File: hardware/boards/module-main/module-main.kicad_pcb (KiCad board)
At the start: 4 copper layers, 48.5 x 108.5 mm, 177 parts, among them J1 2x8 2.54mm shrouded box heade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, J2 2x10 2.54mm pin header, J3 Neutrik NE8FAV, J4 JST B2B-XH-A, Q1 PSMN2R0-30YLE, SW1 NKK M2011SD4G01, U1 LT3042EMSE, U10 OPA2197, U11 OPA2197, U12 OPA2197, U13 ADP7118AUJZ-5.0, U14 RPA20-2412SAW, U15 74AHCT14, U2 LT1641-1IS8, U3 DAC8568ICPW, U4 74AHCT125, U5 OPA2197, U6 INA828IDR, U7 OPA2197, U8 OPA2197IDR, U9 OPA2197

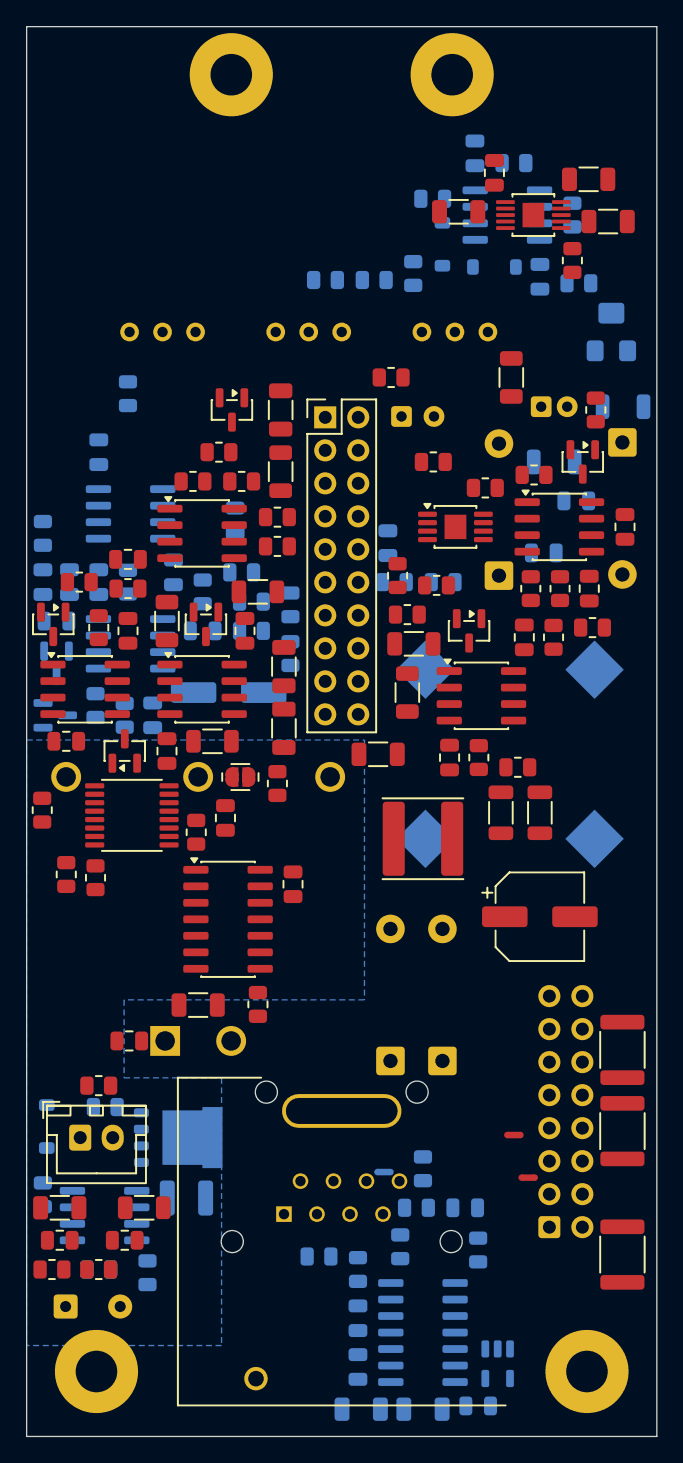
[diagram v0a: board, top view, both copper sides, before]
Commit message: module-main: re-placed - breath receive at the top beside its trimmer, the DAC's LDO beside the DAC, parts spread for routing; placement DRC-clean
Co-Authored-By: Claude Opus 5.5 <noreply@anthropic.com>
Claude-Session: https://claude.ai/code/session_01LmB4muFXnoLprWX4JzuJ5A
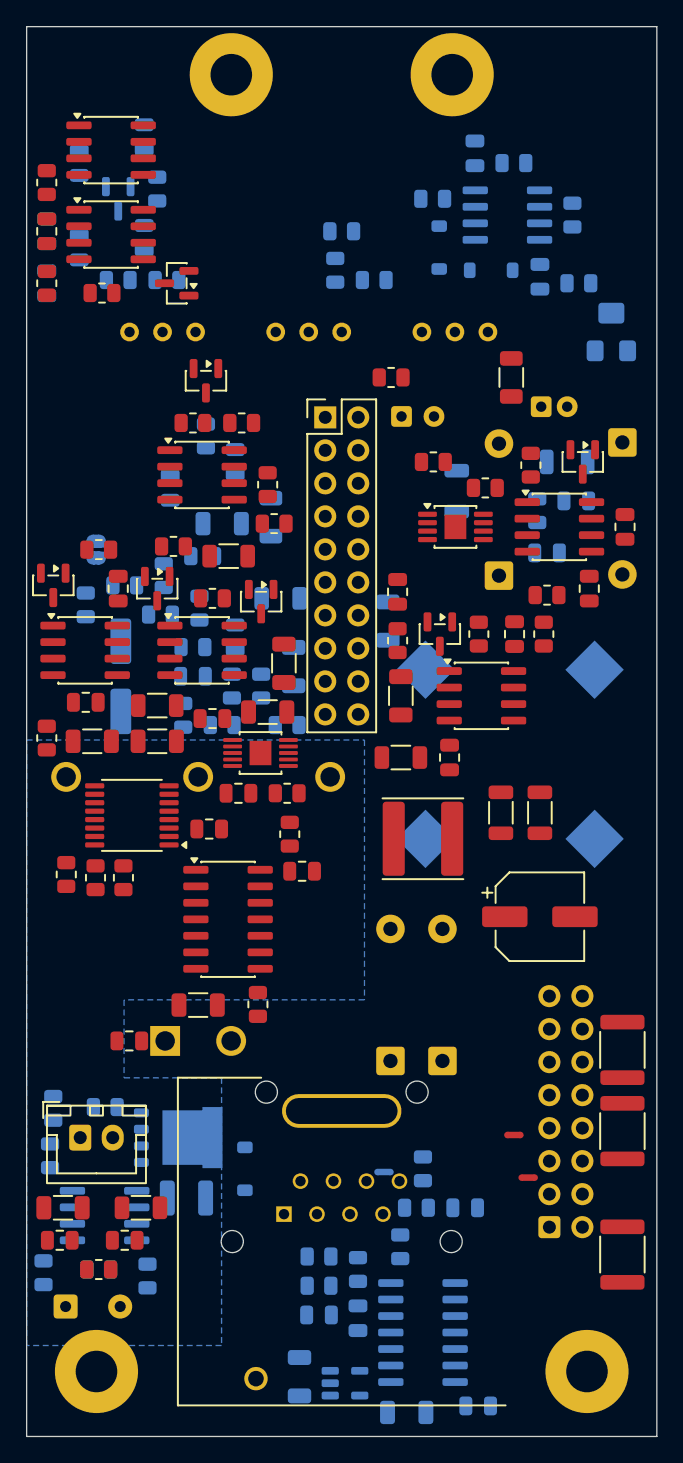
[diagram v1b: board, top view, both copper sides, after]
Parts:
- C13, C29, C43, D4, R16, R17, R19, R40, U5, U6: moved to F.Cu
- C21, C22, C30, C31, C36, C38, JP1, R25, R26, R35, R36, R37, R38, R41, R47, R53, R58, R64, R71: moved to B.Cu
- moved C5 56.4 mm to (66.0, 86.5), turned to 180 degrees
- moved R1 54.7 mm to (62.5, 86.2), turned to 90 degrees
- moved C6 54.5 mm to (71.0, 86.5), turned to 180 degrees
- moved C7 47.3 mm to (75.3, 84.8), turned to 180 degrees
- moved U1 46.4 mm to (79.0, 87.4)
- moved C51 41.2 mm to (79.5, 84.2), turned to 0 degrees
- moved D5 36.1 mm to (68.0, 44.8)
- moved D4 34.5 mm to (72.5, 51.2), turned to 180 degrees
- moved C18 33.6 mm to (70.0, 40.0)
- moved R17 32.7 mm to (62.5, 51.2)
- moved R16 32.5 mm to (66.8, 52.0), turned to 180 degrees
- moved U6 31.5 mm to (67.5, 47.5)
- moved R19 31.4 mm to (62.5, 43.5)
- moved R20 31.2 mm to (71.0, 44.0)
- moved C16 30.6 mm to (70.0, 47.8), turned to -90 degrees
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
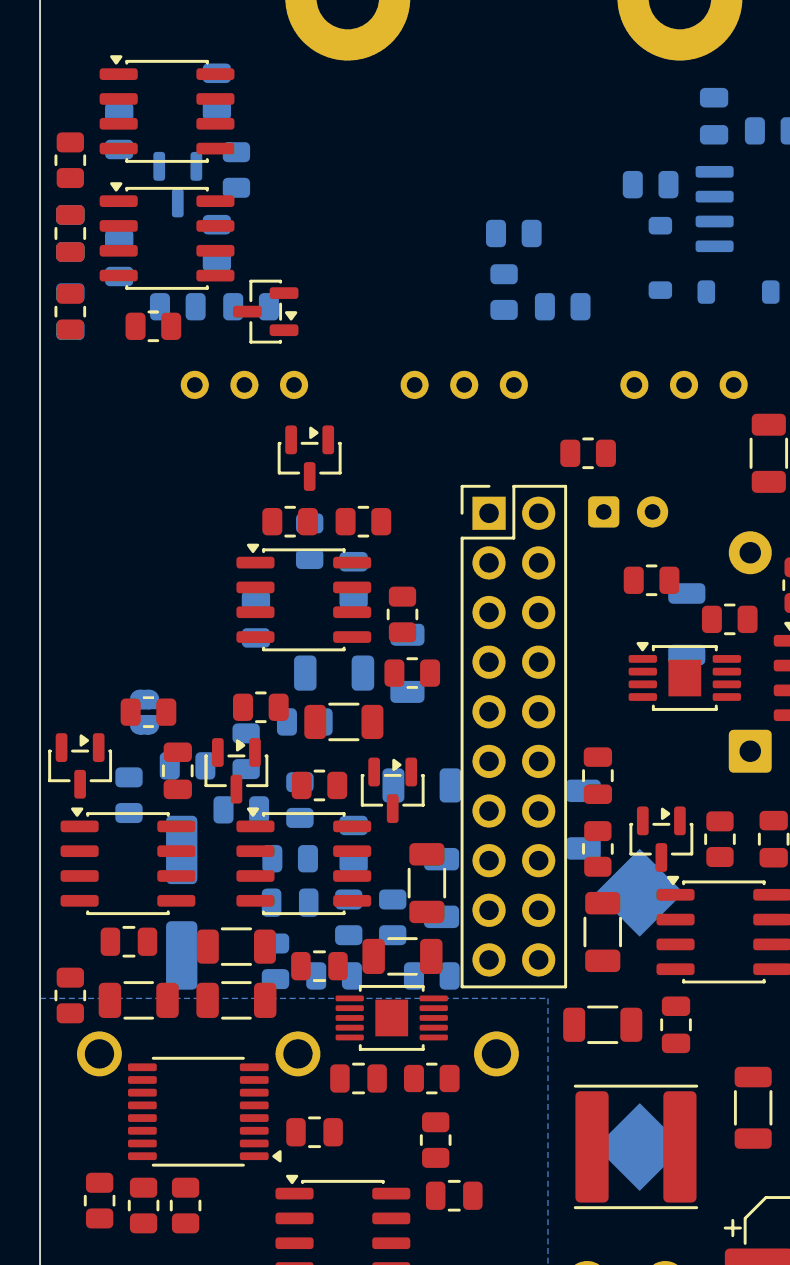
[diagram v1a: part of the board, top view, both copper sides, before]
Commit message: module-main: LDO block to the top middle (R-SET-DAC away from edges, standoffs, connectors; along the long edge), SET guard on both faces, DAC decouplers at their pins
Co-Authored-By: Claude Opus 5.5 <noreply@anthropic.com>
Claude-Session: https://claude.ai/code/session_01LmB4muFXnoLprWX4JzuJ5A
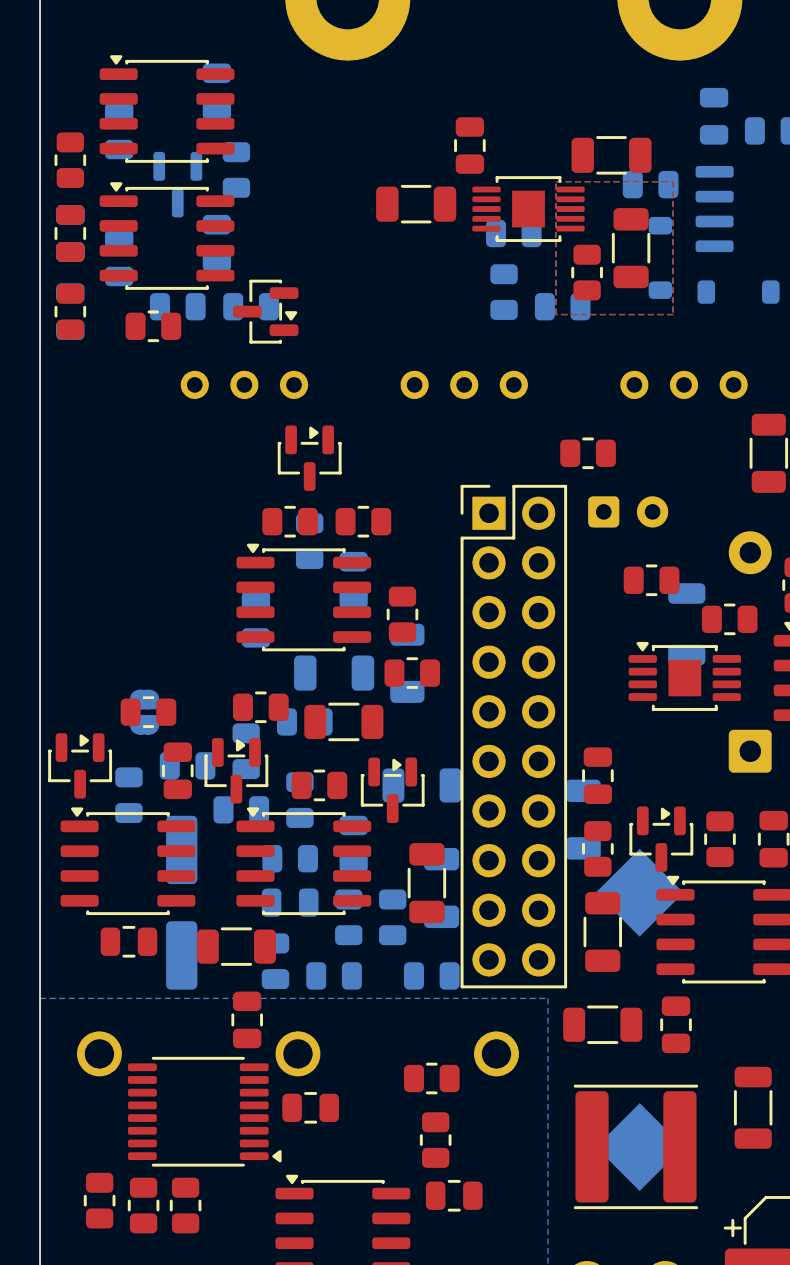
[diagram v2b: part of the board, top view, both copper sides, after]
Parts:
- moved C6 47.3 mm to (90.2, 43.2), turned to 0 degrees
- moved C5 46.0 mm to (91.2, 48.0), turned to -90 degrees
- moved R1 45.5 mm to (89.0, 49.2), turned to -90 degrees
- moved C7 42.7 mm to (83.0, 42.8), turned to 90 degrees
- moved U1 42.0 mm to (86.0, 46.0)
- moved C51 38.5 mm to (80.2, 45.8), turned to 180 degrees
- moved C43 6.44 mm to (71.6, 87.5), turned to 90 degrees
- moved C11 1.27 mm to (74.8, 92.0)
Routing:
- added copper zone on B.Cu, net /DAC_AVDD
- added copper zone on F.Cu, net /DAC_AVDD

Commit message: module-main: routing in progress (resumable run's saved state)
Co-Authored-By: Claude Opus 5.5 <noreply@anthropic.com>
Claude-Session: https://claude.ai/code/session_01LmB4muFXnoLprWX4JzuJ5A
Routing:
- net /AGND_SENSE: track 0.00 -> 89.5 mm
- net AGND_MOD: track 0.00 -> 86.1 mm, vias 0 -> 59
- net /BREATH_SENSE: track 0.00 -> 85.8 mm
- net /DAC_AVDD: track 0.00 -> 80.7 mm, vias 0 -> 8
- net MODULE_ANALOG_POS12: track 0.00 -> 38.7 mm, vias 0 -> 32
- net DIG_GND: track 0.00 -> 21.8 mm, vias 0 -> 21
- net /mod-channels/OUT_1: track 0.00 -> 18.8 mm, vias 0 -> 4
- net PWR_GND: track 0.00 -> 13.4 mm, vias 0 -> 3
- net /mod-channels/VREF_MOD: track 0.00 -> 8.21 mm, vias 0 -> 2
- net /breath-receive-stage/IN_NEG: track 0.00 -> 7.55 mm, vias 0 -> 2
- net MODULE_ANALOG_NEG12: track 0.00 -> 6.26 mm
- net /power-entry/BUS_GND: track 0.00 -> 5.73 mm
- net LOGIC_5V: track 0.00 -> 5.08 mm
- net /PITCH_JACK: track 0.00 -> 4.11 mm
- net /GAIN_FLOOR: track 0.00 -> 3.98 mm, vias 0 -> 1
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
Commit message: module-main: routing in progress (94 connections left); pcb_route.escape for fine-pitch pads
Co-Authored-By: Claude Opus 5.5 <noreply@anthropic.com>
Claude-Session: https://claude.ai/code/session_01LmB4muFXnoLprWX4JzuJ5A
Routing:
- net MODULE_ANALOG_NEG12: track 6.26 -> 181.0 mm, vias 0 -> 21
- net /DAC_AVDD: track 80.7 -> 205.3 mm, vias 8 -> 18
- net LOGIC_5V: track 5.08 -> 49.5 mm, vias 0 -> 6
- net /dac8568/CLR: track 0.00 -> 38.0 mm, vias 0 -> 4
- net /mod-channels/OUT_4: track 1.00 -> 23.5 mm, vias 0 -> 6
- net /mod-channels/MINUS_3: track 1.00 -> 22.6 mm, vias 0 -> 3
- net /UMBILICAL_POS12: track 2.38 -> 23.7 mm, vias 0 -> 7
- net MODULE_ANALOG_POS12: track 38.7 -> 59.3 mm, vias 32 -> 34
- net /digital-and-supervision/SCLK_RC: track 1.33 -> 21.9 mm, vias 0 -> 4
- net /mod-channels/OUT_3: track 0.00 -> 19.7 mm, vias 0 -> 2
- net /pitch-stage/AMP_OUT: track 1.33 -> 18.7 mm, vias 0 -> 2
- net /digital-and-supervision/MOSI_RC: track 0.00 -> 15.6 mm, vias 0 -> 6
- net /umbilical-load-switch/SENSE_NODE: track 1.97 -> 16.5 mm, vias 1 -> 3
- net /breath-output-stage/BREATH_OUT: track 1.45 -> 15.8 mm, vias 1 -> 5
- net /pitch-stage/VREF_SUM: track 0.00 -> 12.3 mm, vias 0 -> 2
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
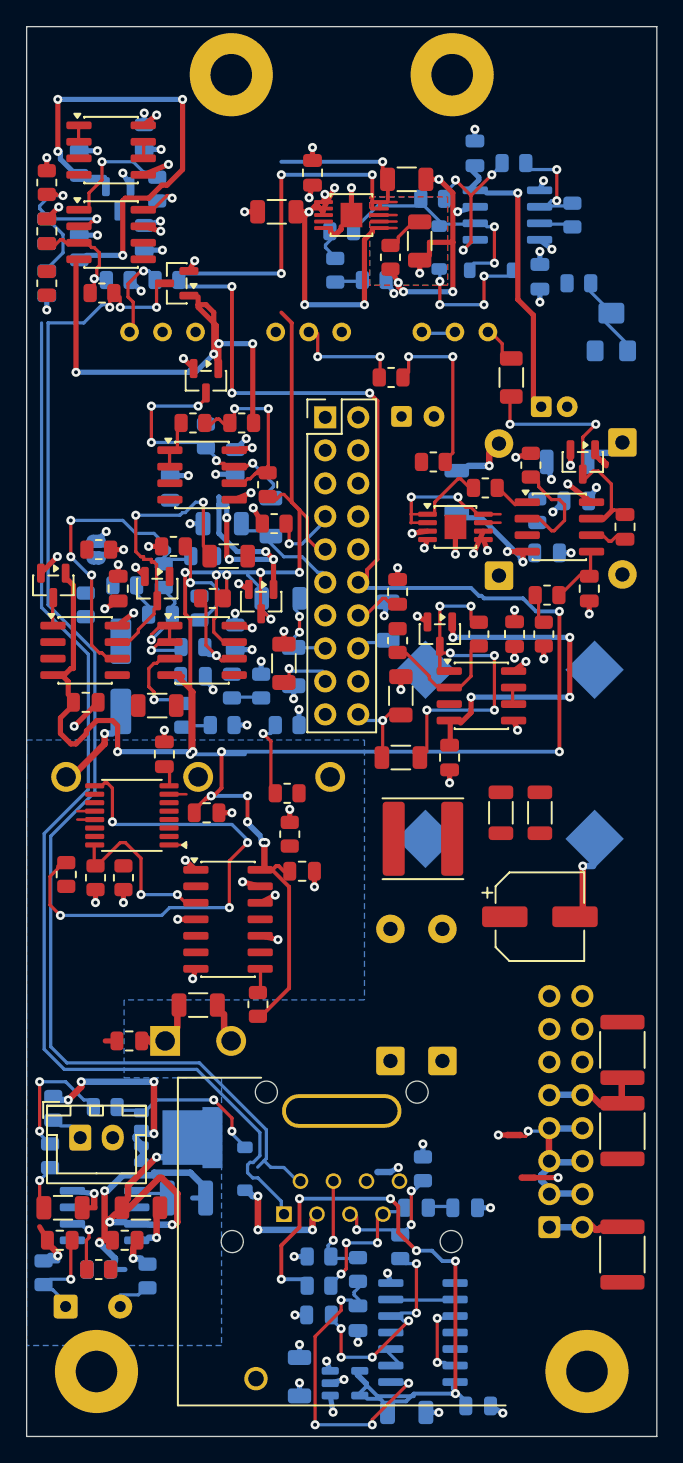
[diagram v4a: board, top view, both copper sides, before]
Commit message: pcb_route: complete routes layer 3 too when layout.yaml directions: names it; module-main routed by it on three directional layers
Co-Authored-By: Claude Opus 5.5 <noreply@anthropic.com>
Claude-Session: https://claude.ai/code/session_01LmB4muFXnoLprWX4JzuJ5A
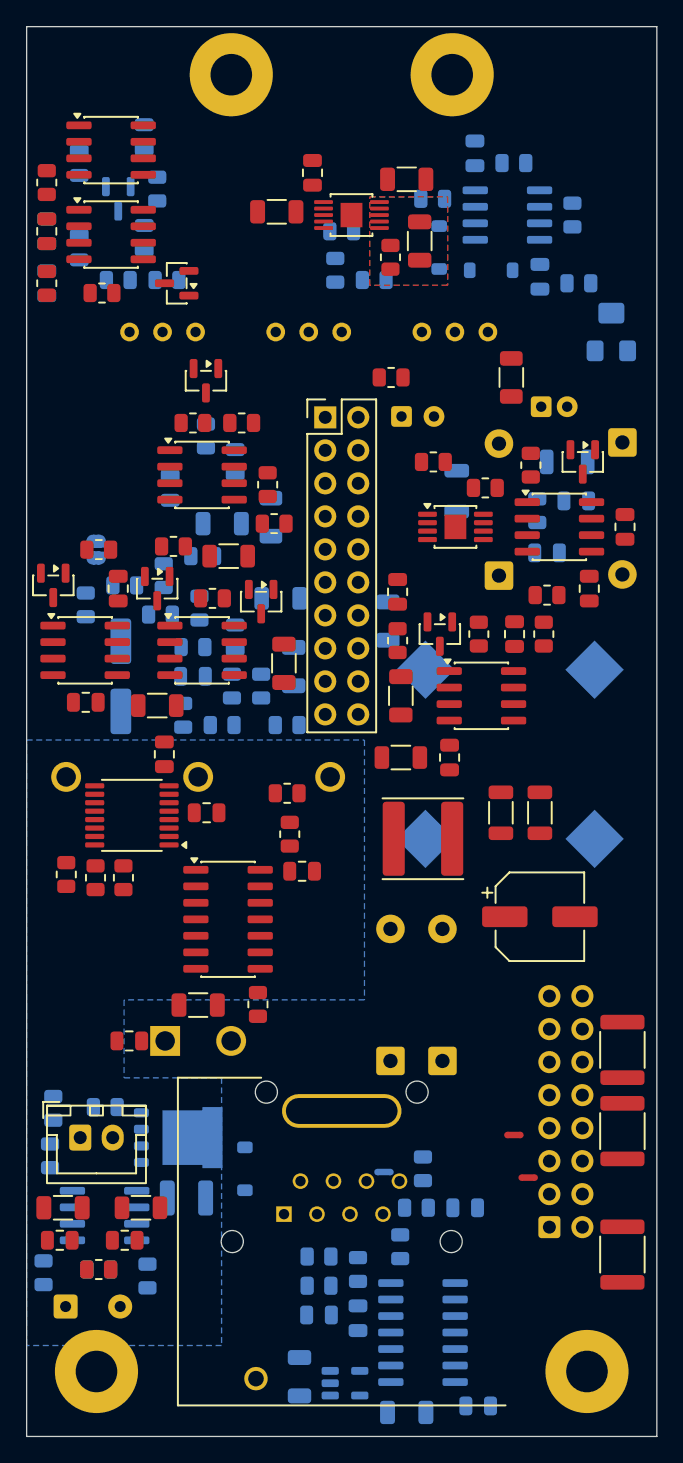
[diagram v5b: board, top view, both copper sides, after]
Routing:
- net /DAC_AVDD: track 205.3 -> 0.00 mm, vias 18 -> 0
- net MODULE_ANALOG_NEG12: track 181.0 -> 0.00 mm, vias 21 -> 0
- net /AGND_SENSE: track 95.1 -> 0.00 mm, vias 3 -> 0
- net AGND_MOD: track 87.5 -> 0.00 mm, vias 59 -> 0
- net /BREATH_SENSE: track 85.8 -> 0.00 mm
- net MODULE_ANALOG_POS12: track 59.3 -> 0.00 mm, vias 34 -> 0
- net LOGIC_5V: track 49.5 -> 0.00 mm, vias 6 -> 0
- net /dac8568/CLR: track 38.0 -> 0.00 mm, vias 4 -> 0
- net PWR_GND: track 25.6 -> 0.00 mm, vias 4 -> 0
- net /UMBILICAL_POS12: track 23.7 -> 0.00 mm, vias 7 -> 0
- net /mod-channels/OUT_4: track 23.5 -> 0.00 mm, vias 6 -> 0
- net /mod-channels/MINUS_3: track 22.6 -> 0.00 mm, vias 3 -> 0
- net /digital-and-supervision/SCLK_RC: track 21.9 -> 0.00 mm, vias 4 -> 0
- net DIG_GND: track 21.8 -> 0.00 mm, vias 21 -> 0
- net /mod-channels/OUT_3: track 19.7 -> 0.00 mm, vias 2 -> 0
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- removed copper zone on In2.Cu, net MODULE_ANALOG_POS12

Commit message: module-main: routing state (three directional layers, in progress); pcb_route: a front and a rear pad at one place get a via, tidy squares outer joins only
Co-Authored-By: Claude Opus 5.5 <noreply@anthropic.com>
Claude-Session: https://claude.ai/code/session_01LmB4muFXnoLprWX4JzuJ5A
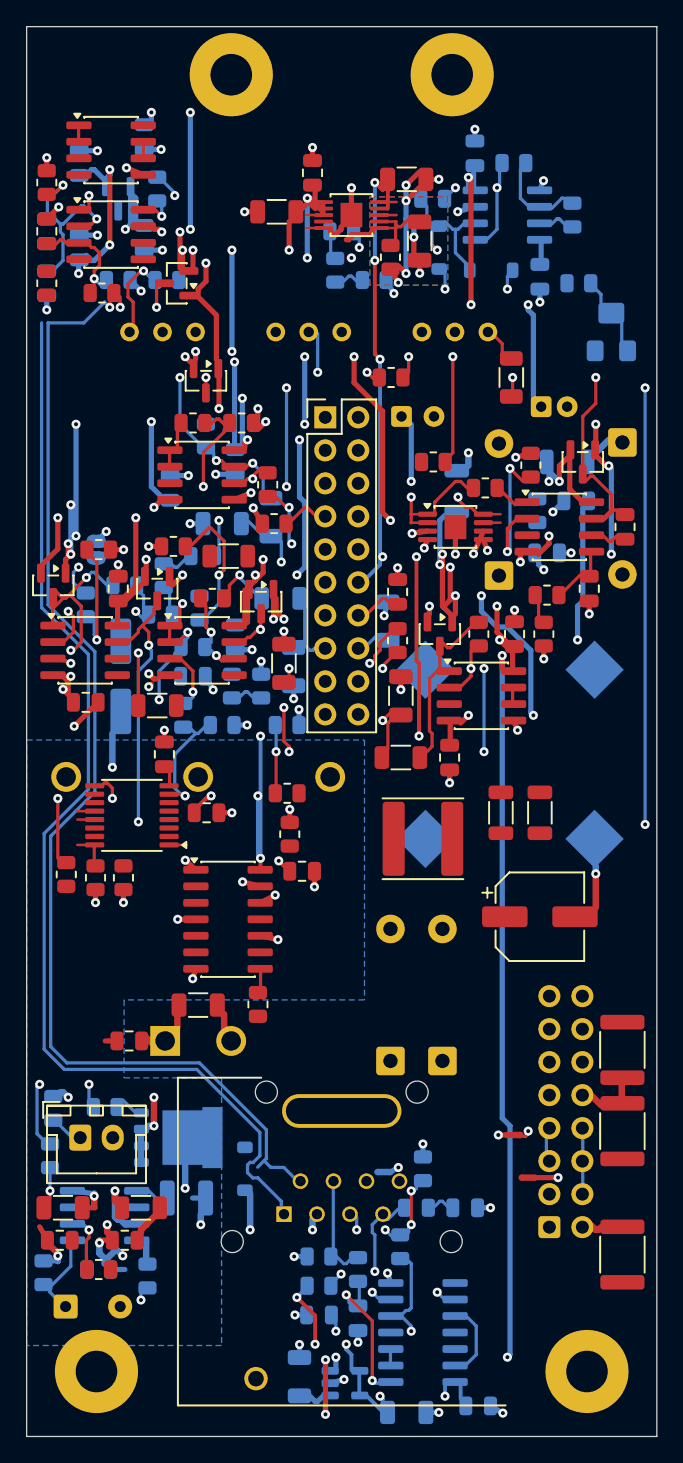
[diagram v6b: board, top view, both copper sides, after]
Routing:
- net MODULE_ANALOG_POS12: track 0.00 -> 281.3 mm, vias 0 -> 38
- net MODULE_ANALOG_NEG12: track 0.00 -> 263.2 mm, vias 0 -> 41
- net /mod-channels/OUT_3: track 0.00 -> 135.9 mm, vias 0 -> 7
- net /AGND_SENSE: track 0.00 -> 95.3 mm, vias 0 -> 3
- net /BREATH_SENSE: track 0.00 -> 85.8 mm
- net AGND_MOD: track 0.00 -> 85.6 mm, vias 0 -> 61
- net /DAC_AVDD: track 0.00 -> 84.7 mm, vias 0 -> 11
- net /mod-channels/VREF_MOD: track 0.00 -> 57.9 mm, vias 0 -> 8
- net PWR_GND: track 0.00 -> 28.0 mm, vias 0 -> 6
- net /mod-channels/OUT_2: track 0.00 -> 22.1 mm, vias 0 -> 3
- net DIG_GND: track 0.00 -> 21.8 mm, vias 0 -> 21
- net /pitch-stage/AMP_OUT: track 0.00 -> 20.7 mm, vias 0 -> 2
- net /UMBILICAL_POS12: track 0.00 -> 20.4 mm, vias 0 -> 5
- net LOGIC_5V: track 0.00 -> 20.3 mm, vias 0 -> 5
- net /breath-response-shaper/VIRTUAL_GND: track 0.00 -> 15.4 mm, vias 0 -> 2
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
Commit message: module-main: routing state, 74 connections left (directional grid router)
Co-Authored-By: Claude Opus 5.5 <noreply@anthropic.com>
Claude-Session: https://claude.ai/code/session_01LmB4muFXnoLprWX4JzuJ5A
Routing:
- net /mod-channels/MINUS_3: track 1.33 -> 146.3 mm, vias 0 -> 8
- net /mod-channels/OUT_3: track 135.9 -> 3.43 mm, vias 7 -> 0
- net /pitch-stage/VREF_BUFFERED: track 1.41 -> 20.2 mm, vias 0 -> 2
- net /UMBILICAL_POS12: track 20.4 -> 35.3 mm, vias 5 -> 8
- net /mod-channels/VREF_MOD: track 57.9 -> 70.3 mm, vias 8 -> 6
- net MODULE_ANALOG_POS12: track 281.3 -> 293.6 mm, vias 38 -> 41
- net /SCLK_DAC: track 2.54 -> 12.6 mm, vias 0 -> 2
- net /DAC_CH4: track 11.3 -> 1.34 mm, vias 1 -> 0
- net /mod-channels/MINUS_1: track 4.30 -> 8.31 mm
- net /mod-channels/OUT_1: track 6.96 -> 4.13 mm, vias 2 -> 1
- net /pitch-stage/VREF_FB: track 10.7 -> 13.4 mm, vias 2 -> 3
- net MODULE_ANALOG_NEG12: track 263.2 -> 260.8 mm, vias 41 -> 47
- net /breath-output-stage/SUM_NODE: track 12.3 -> 14.3 mm, vias 2 -> 3
- net ISO_POS12: track 8.21 -> 9.66 mm, vias 1 -> 2
- net /umbilical-load-switch/ON: track 4.83 -> 6.23 mm, vias 0 -> 1
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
